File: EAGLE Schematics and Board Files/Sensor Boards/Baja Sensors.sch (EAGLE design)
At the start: 9 parts, among them U1 MSP430G2553IN20

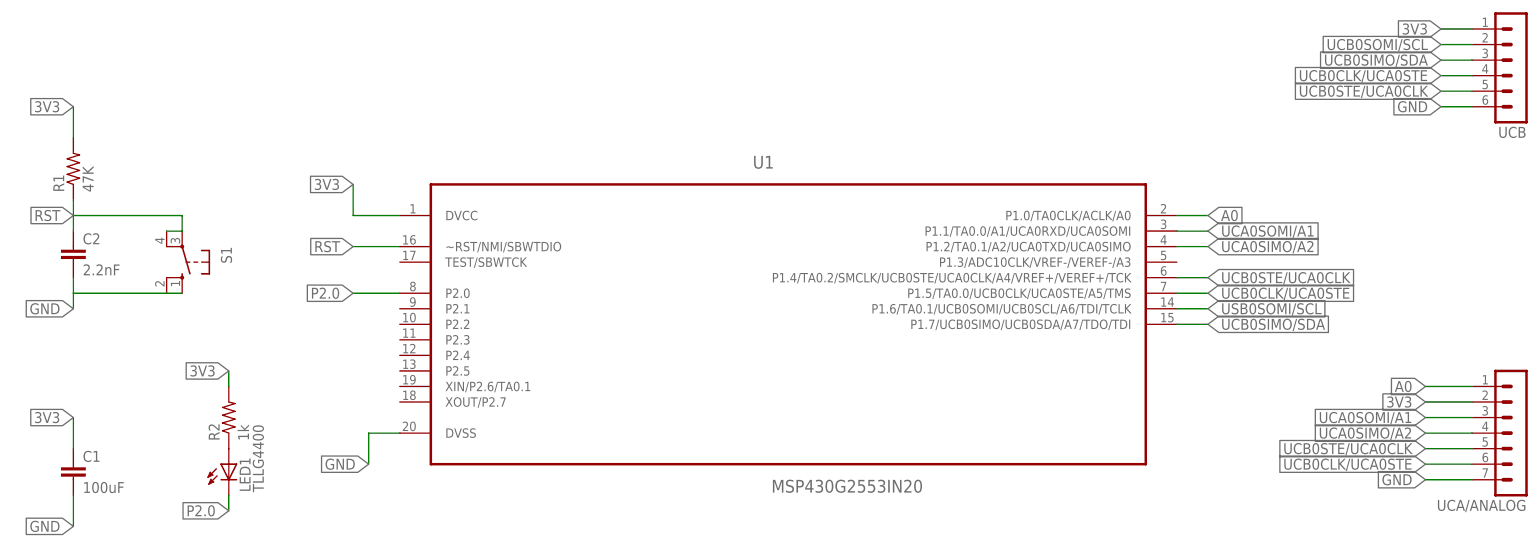
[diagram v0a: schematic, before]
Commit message: New sensor board design & Gerber files
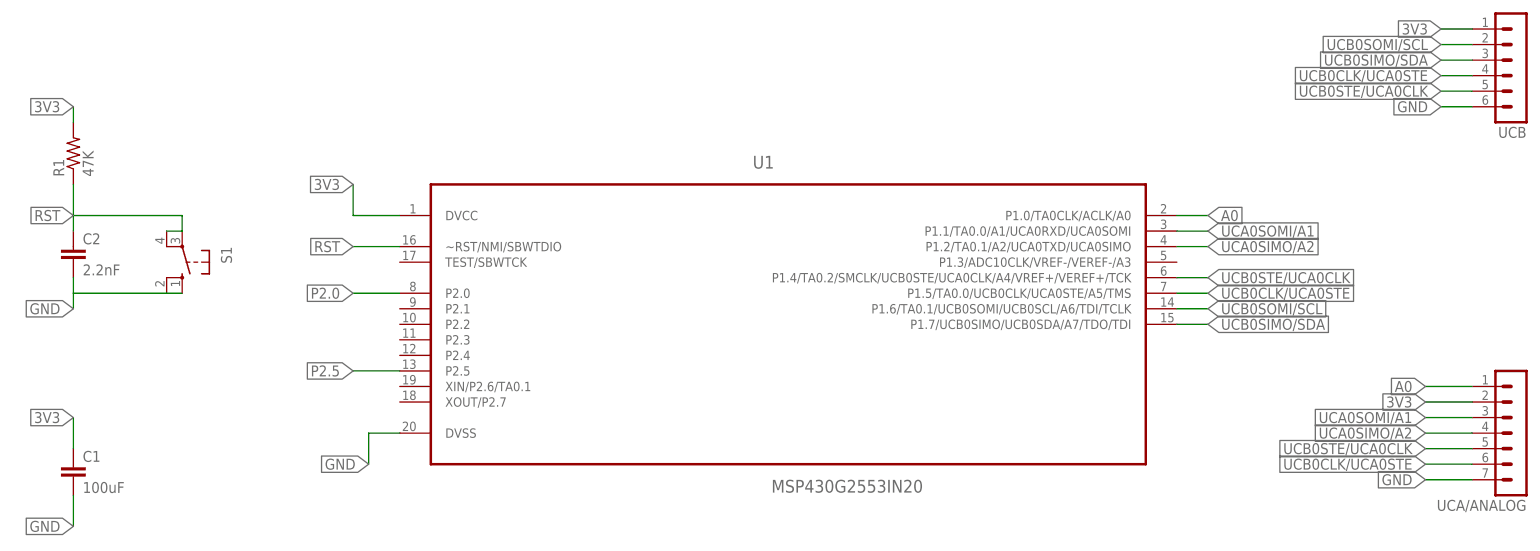
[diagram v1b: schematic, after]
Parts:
- removed LED1: TLLG4400, led:TLLG4400
- removed R2: 1k, rcl:R-US_0207/5V
- C2: device capacitor-wima:C2,5-3 -> capacitor-wima:C5/3
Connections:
- removed net N$1: LED1.A, R2.1
- removed net USB0SOMI/SCL: U1.P1.6/TA0.1/UCB0SOMI/UCB0SCL/A6/TDI/TCLK
- new net P2.5: U1.P2.5
- net 3V3: no longer R2.2
- net P2.0: no longer LED1.C
- net UCB0SOMI/SCL: now also U1.P1.6/TA0.1/UCB0SOMI/UCB0SCL/A6/TDI/TCLK
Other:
- moved on the sheet: R1
